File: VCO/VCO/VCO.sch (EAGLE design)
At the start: 17 parts, among them IC1 AD711N, IC2 AD711N, T1 BC337, T2 BC337

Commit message: Update schematic
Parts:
- added C10, C9: 100n, capacitor-wima:C5/2.5
- added IC3: AD711N, analog-devices:AD711N
- added R10, R11, R15, R16, R8, R9: 100k, eagle-ltspice:R0207/10
- added R12, R13, R14, R17, R5: 47k, rcl:R-TRIMM64W
- added R6, R7: 10K, eagle-ltspice:R0207/10
- added X1, X2, X3: 1503_09, con-lumberg:1503_09
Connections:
- new net N$10: R10.2, R12.S
- new net N$11: R5.E, R6.2
- new net N$12: R14.E, X1.3
- new net N$13: IC3.IN+, R10.1, R11.1, R8.1, R9.1
- new net N$14: R17.E, X3.3
- new net N$15: R11.2, R14.A, R14.S
- new net N$16: R13.A, R13.S, R9.2
- new net N$17: R13.E, X2.3
- new net N$18: IC3.OUT, R1.2, R15.1
- new net N$19: R17.A, R17.S, R8.2
- new net N$20: IC3.IN-, R15.2, R16.1
- new net N$6: IC2.IN+, R5.S
- new net N$9: R5.A, R7.2
- net GND: now also C10.2, C9.1, R12.A, R16.2, R7.1, X1.1, X2.1, X3.1; no longer IC2.IN+
- net VCC: now also C9.2, IC2.+VS, IC3.+VS, R12.E, R6.1; no longer IC2.-VS
- net VEE: now also C10.1, IC2.-VS, IC3.-VS; no longer IC2.+VS
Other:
- note added: "CV1"
- note added: "CV2"
- note added: "CV3"
- note added: "CVoff"
- note added: "Trim Fh"
- moved on the sheet: C1, C4, C5, C6, C7, C8, D1, IC1, IC2, R1, R4

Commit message: Schematic update
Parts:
- added C11: 10u, rcl:CPOL-EUE2.5-7
- added C12, C13, C14, C15: 100n, capacitor-wima:C5/2.5
- added IC4, IC5: AD711N, analog-devices:AD711N
- added R18: 10K, eagle-ltspice:R0207/10
- added R19, R23, R24: 10k, resistor:R-TRIMM3339P
- added R20, R21, R22: 100k, eagle-ltspice:R0207/10
- added X4, X5, X6: 1503_09, con-lumberg:1503_09
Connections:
- new net N$21: IC5.IN-, R19.S, X4.3
- new net N$22: IC5.OUT, R24.E
- new net N$23: R24.S, X6.3
- new net N$24: IC4.IN-, R20.1, R21.1, R22.2
- new net N$25: C11.-, R18.2, R19.E
- new net N$27: R20.2, X5.3
- new net N$28: R21.2, R23.S
- new net N$29: IC4.OUT, IC5.IN+, R22.1
- net GND: now also C12.1, C13.2, C14.1, C15.2, IC4.IN+, R18.1, R19.A, R24.A, X4.1, X5.1, X6.1
- net N$8: now also C11.+
- net VCC: now also C12.2, C14.2, IC4.+VS, IC5.+VS, R23.E
- net VEE: now also C13.1, C15.1, IC4.-VS, IC5.-VS, R23.A
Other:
- moved on the sheet: C4, R4

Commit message: Schema update
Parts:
- removed X1, X2, X3, X4, X5, X6: 1503_09, con-lumberg:1503_09
- added PAD1: CV1, wirepad:3,17/1,1
- added PAD2: CV2, wirepad:3,17/1,1
- added PAD3: CV3, wirepad:3,17/1,1
- added PAD4: PW, wirepad:3,17/1,1
- added PAD5: SAW, wirepad:3,17/1,1
- added PAD6: PULSE, wirepad:3,17/1,1
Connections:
- net GND: no longer X1.1, X2.1, X3.1, X4.1, X5.1, X6.1
- net N$12: now also PAD1.P; no longer X1.3
- net N$14: now also PAD3.P; no longer X3.3
- net N$17: now also PAD2.P; no longer X2.3
- net N$21: now also PAD5.P; no longer X4.3
- net N$23: now also PAD6.P; no longer X6.3
- net N$27: now also PAD4.P; no longer X5.3
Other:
- note removed: "CV1"
- note removed: "CV2"
- note removed: "CV3"
- moved on the sheet: R23

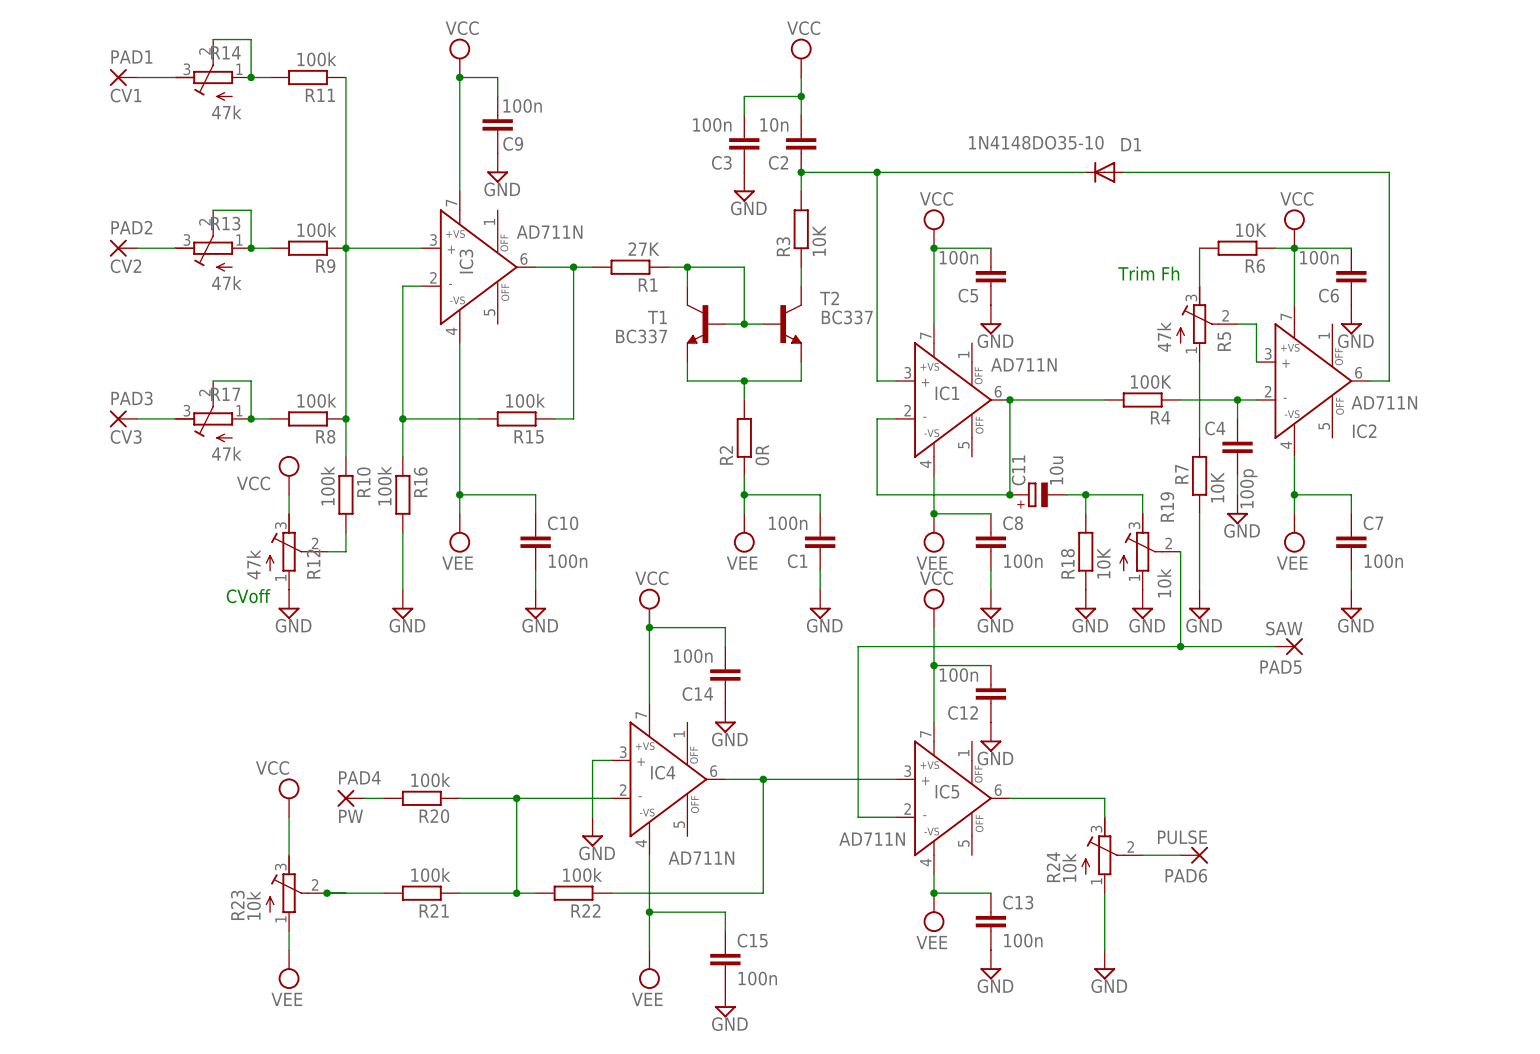
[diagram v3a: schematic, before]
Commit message: schematic update
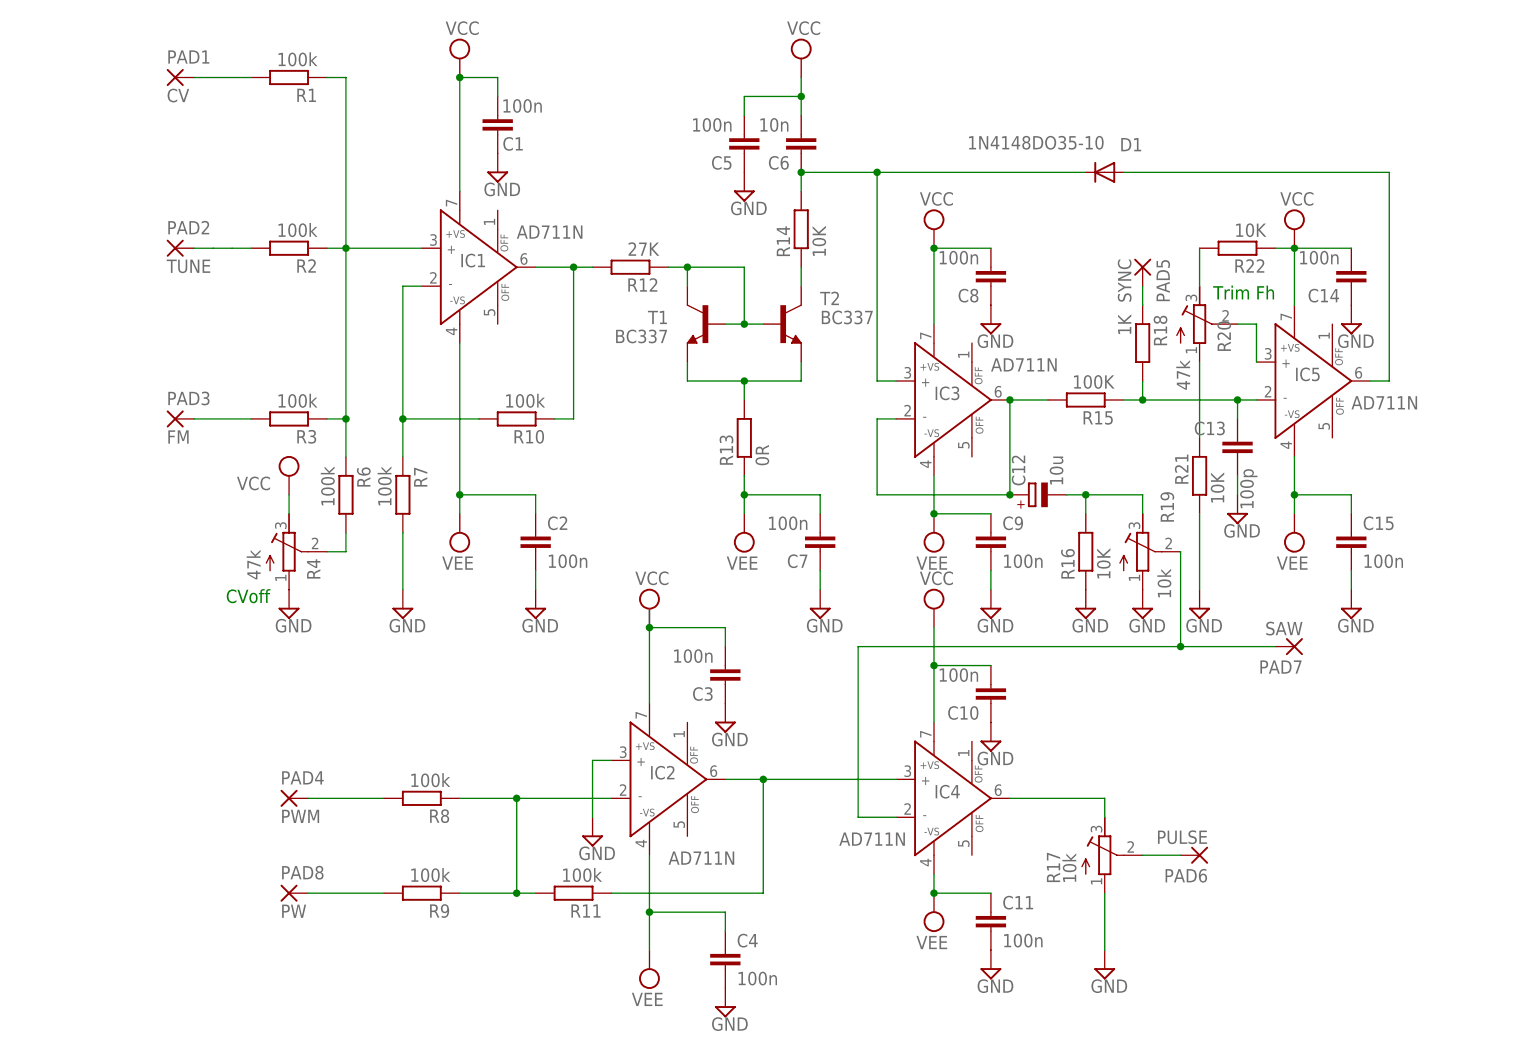
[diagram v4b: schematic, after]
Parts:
- removed R23, R24: 10k, resistor:R-TRIMM3339P
- removed R5: 47k, rcl:R-TRIMM64W
- added PAD7: SAW, wirepad:3,17/1,1
- added PAD8: PW, wirepad:3,17/1,1
- C11: value 10u -> 100n; device rcl:CPOL-EUE2.5-7 -> capacitor-wima:C5/2.5
- C12: value 100n -> 10u; device capacitor-wima:C5/2.5 -> rcl:CPOL-EUE2.5-7
- C13: value 100n -> 100p; device capacitor-wima:C5/2.5 -> capacitor-wima:C2.5/2
- C2: value 10n -> 100n
- C4: value 100p -> 100n; device capacitor-wima:C2.5/2 -> capacitor-wima:C5/2.5
- C6: value 100n -> 10n
- PAD1: value CV1 -> CV
- PAD2: value CV2 -> TUNE
- PAD3: value CV3 -> FM
- PAD4: value PW -> PWM
- PAD5: value SAW -> SYNC
- R1: value 27K -> 100k
- R12: value 47k -> 27K; device rcl:R-TRIMM64W -> eagle-ltspice:R0207/10; SPICEPREFIX (none) -> 27K
- R13: value 47k -> 0R; device rcl:R-TRIMM64W -> eagle-ltspice:R0207/10
- R14: value 47k -> 10K; device rcl:R-TRIMM64W -> eagle-ltspice:R0207/10; SPICEPREFIX (none) -> 10K
- R15: value 100k -> 100K; SPICEPREFIX 27K -> (none)
- R16, R21, R22: value 100k -> 10K; SPICEPREFIX 27K -> 10K
- R17: value 47k -> 10k; device rcl:R-TRIMM64W -> resistor:R-TRIMM3339P
- R18: value 10K -> 1K; SPICEPREFIX 10K -> (none)
- R2: value 0R -> 100k; SPICEPREFIX (none) -> 27K
- R20: value 100k -> 47k; device eagle-ltspice:R0207/10 -> rcl:R-TRIMM64W; SPICEPREFIX 27K -> (none)
- R3, R6, R7: value 10K -> 100k; SPICEPREFIX 10K -> 27K
- R4: value 100K -> 47k; device eagle-ltspice:R0207/10 -> rcl:R-TRIMM64W
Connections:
- removed net N$15: R11.2, R14.A, R14.S
- removed net N$16: R13.A, R13.S, R9.2
- removed net N$19: R17.A, R17.S, R8.2
- new net N$26: PAD5.P, R18.1
- net GND: now also C10.1, C11.2, C13.1, C2.2, C4.2, C7.1, C8.1, C9.2, IC2.IN+, R16.1, R17.A, R21.1, R4.A, R7.2; no longer C10.2, C12.1, C13.2, C4.1, C6.1, C7.2, C8.2, C9.1, IC4.IN+, R12.A, R16.2, R18.1, R24.A, R7.1
- net N$1: now also R12.1; no longer R1.1
- net N$10: now also R4.S, R6.2; no longer R10.2, R12.S
- net N$11: now also R20.E, R22.2; no longer R5.E, R6.2
- net N$12: now also R1.2; no longer R14.E
- net N$13: now also IC1.IN+, R1.1, R2.1, R3.1, R6.1; no longer IC3.IN+, R10.1, R11.1, R8.1, R9.1
- net N$14: now also R3.2; no longer R17.E
- net N$17: now also R2.2; no longer R13.E
- net N$18: now also IC1.OUT, R10.1, R12.2; no longer IC3.OUT, R1.2, R15.1
- net N$2: now also R13.2; no longer R2.2
- net N$20: now also IC1.IN-, R10.2, R7.1; no longer IC3.IN-, R15.2, R16.1
- net N$21: now also IC4.IN-, PAD7.P; no longer IC5.IN-, PAD5.P
- net N$22: now also IC4.OUT, R17.E; no longer IC5.OUT, R24.E
- net N$23: now also R17.S; no longer R24.S
- net N$24: now also IC2.IN-, R11.2, R8.1, R9.1; no longer IC4.IN-, R20.1, R21.1, R22.2
- net N$25: now also C12.-, R16.2; no longer C11.-, R18.2
- net N$27: now also R8.2; no longer R20.2
- net N$28: now also PAD8.P, R9.2; no longer R21.2, R23.S
- net N$29: now also IC2.OUT, IC4.IN+, R11.1; no longer IC4.OUT, IC5.IN+, R22.1
- net N$3: now also C6.1, IC3.IN+, R14.2; no longer C2.1, IC1.IN+, R3.2
- net N$4: now also R14.1; no longer R3.1
- net N$5: now also IC5.OUT; no longer IC2.OUT
- net N$6: now also IC5.IN+, R20.S; no longer IC2.IN+, R5.S
- net N$7: now also C13.2, IC5.IN-, R15.1, R18.2; no longer C4.2, IC2.IN-, R4.1
- net N$8: now also C12.+, IC3.IN-, IC3.OUT, R15.2; no longer C11.+, IC1.IN-, IC1.OUT, R4.2
- net N$9: now also R20.A, R21.2; no longer R5.A, R7.2
- net VCC: now also C1.2, C10.2, C8.2, R22.1, R4.E; no longer C12.2, C2.2, C9.2, R12.E, R23.E, R6.1
- net VEE: now also C11.1, C2.1, C4.1, C7.2, C9.1, R13.1; no longer C1.2, C10.1, C13.1, C7.1, C8.1, R2.1, R23.A
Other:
- moved on the sheet: C1, C10, C13, C14, C15, C2, C3, C4, C5, C6, C7, C8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

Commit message: Board first layout
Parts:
- added C16, C17: 10u, rcl:CPOL-EUE2.5-7
- added PAD10, PAD11, PAD9: CV, wirepad:3,17/1,1
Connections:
- net GND: now also C16.-, C17.+, PAD11.P
- net VCC: now also C16.+, PAD9.P
- net VEE: now also C17.-, PAD10.P
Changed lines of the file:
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@@
 <grid distance="0.1" unitdist="inch" unit="inch" style="lines" multiple="1" display="no" altdistance="0.01" altunitdist="inch" altunit="inch"/>
 <layers>
-<layer number="1" name="Top" color="4" fill="1" visible="yes" active="no"/>
-<layer number="16" name="Bottom" color="1" fill="1" visible="yes" active="no"/>
-<layer number="17" name="Pads" color="2" fill="1" visible="yes" active="no"/>
-<layer number="18" name="Vias" color="2" fill="1" visible="yes" active="no"/>
-<layer number="19" name="Unrouted" color="6" fill="1" visible="yes" active="no"/>
-<layer number="20" name="Dimension" color="15" fill="1" visible="yes" active="no"/>
-<layer number="21" name="tPlace" color="7" fill="1" visible="yes" active="no"/>
-<layer number="22" name="bPlace" color="7" fill="1" visible="yes" active="no"/>
-<layer number="23" name="tOrigins" color="15" fill="1" visible="yes" active="no"/>
-<layer number="24" name="bOrigins" color="15" fill="1" visible="yes" active="no"/>
-<layer number="25" name="tNames" color="7" fill="1" visible="yes" active="no"/>
-<layer number="26" name="bNames" color="7" fill="1" visible="yes" active="no"/>
-<layer number="27" name="tValues" color="7" fill="1" visible="yes" active="no"/>
-<layer number="28" name="bValues" color="7" fill="1" visible="yes" active="no"/>
+<layer number="1" name="Top" color="4" fill="1" visible="no" active="no"/>
+<layer number="16" name="Bottom" color="1" fill="1" visible="no" active="no"/>
+<layer number="17" name="Pads" color="2" fill="1" visible="no" active="no"/>
+<layer number="18" name="Vias" color="2" fill="1" visible="no" active="no"/>
+<layer number="19" name="Unrouted" color="6" fill="1" visible="no" active="no"/>
+<layer number="20" name="Dimension" color="15" fill="1" visible="no" active="no"/>
+<layer number="21" name="tPlace" color="7" fill="1" visible="no" active="no"/>
+<layer number="22" name="bPlace" color="7" fill="1" visible="no" active="no"/>
+<layer number="23" name="tOrigins" color="15" fill="1" visible="no" active="no"/>
+<layer number="24" name="bOrigins" color="15" fill="1" visible="no" active="no"/>
+<layer number="25" name="tNames" color="7" fill="1" visible="no" active="no"/>
+<layer number="26" name="bNames" color="7" fill="1" visible="no" active="no"/>
+<layer number="27" name="tValues" color="7" fill="1" visible="no" active="no"/>
+<layer number="28" name="bValues" color="7" fill="1" visible="no" active="no"/>
 <layer number="29" name="tStop" color="7" fill="3" visible="no" active="no"/>
 <layer number="30" name="bStop" color="7" fill="6" visible="no" active="no"/>
@@
 <layer number="35" name="tGlue" color="7" fill="4" visible="no" active="no"/>
 <layer number="36" name="bGlue" color="7" fill="5" visible="no" active="no"/>
-<layer number="37" name="tTest" color="7" fill="1" visible="yes" active="no"/>
-<layer number="38" name="bTest" color="7" fill="1" visible="yes" active="no"/>
+<layer number="37" name="tTest" color="7" fill="1" visible="no" active="no"/>
+<layer number="38" name="bTest" color="7" fill="1" visible="no" active="no"/>
 <layer number="39" name="tKeepout" color="4" fill="11" visible="no" active="no"/>
 <layer number="40" name="bKeepout" color="1" fill="11" visible="no" active="no"/>
@@
 <layer number="44" name="Drills" color="7" fill="1" visible="no" active="no"/>
 <layer number="45" name="Holes" color="7" fill="1" visible="no" active="no"/>
-<layer number="46" name="Milling" color="3" fill="1" visible="yes" active="no"/>
-<layer number="47" name="Measures" color="7" fill="1" visible="yes" active="no"/>
-<layer number="48" name="Document" color="7" fill="1" visible="yes" active="no"/>
-<layer number="49" name="Reference" color="7" fill="1" visible="yes" active="no"/>
-<layer number="51" name="tDocu" color="7" fill="1" visible="yes" active="no"/>
-<layer number="52" name="bDocu" color="7" fill="1" visible="yes" active="no"/>
+<layer number="46" name="Milling" color="3" fill="1" visible="no" active="no"/>
+<layer number="47" name="Measures" color="7" fill="1" visible="no" active="no"/>
+<layer number="48" name="Document" color="7" fill="1" visible="no" active="no"/>
+<layer number="49" name="Reference" color="7" fill="1" visible="no" active="no"/>
+<layer number="51" name="tDocu" color="7" fill="1" visible="no" active="no"/>
+<layer number="52" name="bDocu" color="7" fill="1" visible="no" active="no"/>
 <layer number="90" name="Modules" color="5" fill="1" visible="yes" active="yes"/>
 <layer number="91" name="Nets" color="2" fill="1" visible="yes" active="yes"/>
@@
 </part>
 <part name="PAD8" library="wirepad" deviceset="3,17/1,1" device="" value="PW"/>
+<part name="PAD9" library="wirepad" deviceset="3,17/1,1" device="" value="CV"/>
+<part name="PAD10" library="wirepad" deviceset="3,17/1,1" device="" value="CV"/>
+<part name="SUPPLY3" library="supply2" deviceset="VCC" device=""/>
+<part name="SUPPLY4" library="supply2" deviceset="VEE" device=""/>
+<part name="PAD11" library="wirepad" deviceset="3,17/1,1" device="" value="CV"/>
+<part name="SUPPLY36" library="supply2" deviceset="GND" device=""/>
+<part name="C16" library="rcl" deviceset="CPOL-EU" device="E2.5-7" value="10u"/>
+<part name="C17" library="rcl" deviceset="CPOL-EU" device="E2.5-7" value="10u"/>
 </parts>
 <sheets>
@@
 </instance>
 <instance part="PAD8" gate="1" x="-20.32" y="-25.4"/>
+<instance part="PAD9" gate="1" x="-55.88" y="-2.54"/>
+<instance part="PAD10" gate="1" x="-55.88" y="-17.78"/>
+<instance part="SUPPLY3" gate="G$1" x="-45.72" y="5.08" smashed="yes">
+<attribute name="VALUE" x="-47.625" y="8.255" size="1.778" layer="96"/>
+</instance>
+<instance part="SUPPLY4" gate="G$1" x="-45.72" y="-25.4" rot="R180"/>
+<instance part="PAD11" gate="1" x="-55.88" y="-10.16"/>
+<instance part="SUPPLY36" gate="GND" x="-33.02" y="-12.7"/>
+<instance part="C16" gate="G$1" x="-43.18" y="-2.54" rot="R90"/>
+<instance part="C17" gate="G$1" x="-40.64" y="-17.78" rot="R270"/>
 </instances>
 <busses>
@@
 <wire x1="20.32" y1="-7.62" x2="22.86" y2="-7.62" width="0.1524" layer="91"/>
 </segment>
+<segment>
+<pinref part="PAD11" gate="1" pin="P"/>
+<pinref part="SUPPLY36" gate="GND" pin="GND"/>
+<wire x1="-53.34" y1="-10.16" x2="-38.1" y2="-10.16" width="0.1524" layer="91"/>
+<pinref part="C17" gate="G$1" pin="+"/>
+<wire x1="-38.1" y1="-10.16" x2="-33.02" y2="-10.16" width="0.1524" layer="91"/>
+<wire x1="-38.1" y1="-17.78" x2="-38.1" y2="-10.16" width="0.1524" layer="91"/>
+<pinref part="C16" gate="G$1" pin="-"/>
+<wire x1="-38.1" y1="-10.16" x2="-38.1" y2="-2.54" width="0.1524" layer="91"/>
+<junction x="-38.1" y="-10.16"/>
+</segment>
 </net>
 <net name="VCC" class="0">
@@
 <pinref part="SUPPLY11" gate="G$1" pin="VCC"/>
 <junction x="27.94" y="10.16"/>
+</segment>
+<segment>
+<pinref part="PAD9" gate="1" pin="P"/>
+<wire x1="-53.34" y1="-2.54" x2="-45.72" y2="-2.54" width="0.1524" layer="91"/>
+<pinref part="SUPPLY3" gate="G$1" pin="VCC"/>
+<wire x1="-45.72" y1="-2.54" x2="-45.72" y2="2.54" width="0.1524" layer="91"/>
+<pinref part="C16" gate="G$1" pin="+"/>
+<junction x="-45.72" y="-2.54"/>
 </segment>
 </net>
@@
 <junction x="27.94" y="-27.94"/>
 </segment>
+<segment>
+<pinref part="PAD10" gate="1" pin="P"/>
+<wire x1="-53.34" y1="-17.78" x2="-45.72" y2="-17.78" width="0.1524" layer="91"/>
+<pinref part="SUPPLY4" gate="G$1" pin="VEE"/>
+<wire x1="-45.72" y1="-17.78" x2="-45.72" y2="-22.86" width="0.1524" layer="91"/>
+<pinref part="C17" gate="G$1" pin="-"/>
+<junction x="-45.72" y="-17.78"/>
+</segment>
 </net>
